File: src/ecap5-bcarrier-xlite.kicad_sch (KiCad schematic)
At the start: 41 parts, among them J3 Conn_01x04, J4 Conn_01x04, J5 USB_C_Receptacle_USB2.0_14P, J6 Conn_Coaxial, J7 Conn_Coaxial, J8 Conn_Coaxial, J9 1935161, Q1 BC846BR13, Q2 BC846BR13, SW1 RESET_SOM1, SW2 RESET_SOM2, SW3 USER1, SW4 USER1, U2 AP7375-33SA-7

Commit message: Route more
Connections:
- net GND: now also Q1.2 (E), Q2.2 (E); no longer Q1.E, Q2.E
- net at R11.1: now also Q2.1 (B); no longer Q2.B
- net at D8.1 (K): now also Q2.3 (C); no longer Q2.C
- net at D2.1 (K): now also Q1.3 (C); no longer Q1.C
- net at R9.1: now also Q1.1 (B); no longer Q1.B
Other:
- sheet SOM1 ports: added RTD0N, RTD0P, SE65; removed none
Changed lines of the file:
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@@
 	(wire
 		(pts
-			(xy 247.65 48.26) (xy 231.14 48.26)
+			(xy 241.3 48.26) (xy 224.79 48.26)
 		)
 		(stroke
@@
 	(wire
 		(pts
-			(xy 247.65 43.18) (xy 231.14 43.18)
+			(xy 241.3 43.18) (xy 224.79 43.18)
 		)
 		(stroke
@@
 	(wire
 		(pts
+			(xy 241.3 54.61) (xy 224.79 54.61)
+		)
+		(stroke
+			(width 0)
+			(type default)
+		)
+	)
+	(wire
+		(pts
 			(xy 52.07 74.93) (xy 57.15 74.93)
 		)
@@
 	(wire
 		(pts
-			(xy 247.65 45.72) (xy 231.14 45.72)
+			(xy 241.3 45.72) (xy 224.79 45.72)
 		)
 		(stroke
@@
 	(wire
 		(pts
+			(xy 241.3 58.42) (xy 224.79 58.42)
+		)
+		(stroke
+			(width 0)
+			(type default)
+		)
+	)
+	(wire
+		(pts
 			(xy 29.21 105.41) (xy 36.83 105.41)
 		)
@@
 	(wire
 		(pts
+			(xy 241.3 36.83) (xy 224.79 36.83)
+		)
+		(stroke
+			(width 0)
+			(type default)
+		)
+	)
+	(wire
+		(pts
 			(xy 158.75 153.67) (xy 154.94 153.67)
 		)
@@
 	(wire
 		(pts
+			(xy 241.3 52.07) (xy 224.79 52.07)
+		)
+		(stroke
+			(width 0)
+			(type default)
+		)
+	)
+	(wire
+		(pts
 			(xy 182.88 128.27) (xy 182.88 130.81)
 		)
@@
 	(wire
 		(pts
+			(xy 285.75 36.83) (xy 269.24 36.83)
+		)
+		(stroke
+			(width 0)
+			(type default)
+		)
+	)
+	(wire
+		(pts
 			(xy 250.19 149.86) (xy 254 149.86)
 		)
@@
 	(wire
 		(pts
-			(xy 247.65 40.64) (xy 231.14 40.64)
+			(xy 241.3 40.64) (xy 224.79 40.64)
 		)
 		(stroke
@@
 	)
 	(label "SOM1.JTAC_TDI"
-		(at 247.65 43.18 180)
+		(at 241.3 43.18 180)
 		(effects
 			(font
@@
 	)
 	(label "TP.SINGLEENDED"
-		(at 173.99 90.17 180)
+		(at 241.3 58.42 180)
 		(effects
 			(font
@@
 	)
 	(label "SOM1.JTAC_TCK"
-		(at 247.65 40.64 180)
+		(at 241.3 40.64 180)
 		(effects
 			(font
@@
 	)
 	(label "SOM1.JTAC_TMS"
-		(at 247.65 48.26 180)
+		(at 241.3 48.26 180)
 		(effects
 			(font
@@
 	)
 	(label "SOM1.JTAC_TDO"
-		(at 247.65 45.72 180)
+		(at 241.3 45.72 180)
 		(effects
 			(font
@@
 	)
 	(label "TP.DIFFN"
-		(at 173.99 95.25 180)
+		(at 241.3 54.61 180)
 		(effects
 			(font
@@
 	)
 	(label "TP.DIFFP"
-		(at 173.99 92.71 180)
+		(at 241.3 52.07 180)
 		(effects
 			(font
@@
 	)
 	(label "SOM2.RESET_IN"
-		(at 173.99 72.39 180)
+		(at 285.75 36.83 180)
 		(effects
 			(font
@@
 	)
 	(label "SOM1.RESET_IN"
-		(at 173.99 69.85 180)
+		(at 241.3 36.83 180)
 		(effects
 			(font
@@
 	)
 	(symbol
-		(lib_id "Device:Q_NPN")
-		(at 222.25 153.67 0)
-		(mirror y)
-		(unit 1)
-		(exclude_from_sim no)
-		(in_bom yes)
-		(on_board yes)
-		(dnp no)
-		(fields_autoplaced yes)
-		(property "Reference" "Q2"
-			(at 217.17 152.3999 0)
-			(effects
-				(font
-					(size 1.27 1.27)
-				)
-				(justify left)
-			)
-		)
-		(property "Value" "BC846BR13"
-			(at 217.17 154.9399 0)
-			(effects
-				(font
-					(size 1.27 1.27)
-				)
-				(justify left)
-			)
-		)
-		(property "Footprint" "Package_TO_SOT_SMD:SOT-23-3"
-			(at 217.17 151.13 0)
-			(effects
-				(font
-					(size 1.27 1.27)
-				)
-				(hide yes)
-			)
-		)
-		(property "Datasheet" "~"
-			(at 222.25 153.67 0)
-			(effects
-				(font
-					(size 1.27 1.27)
-				)
-				(hide yes)
-			)
-		)
-		(property "Description" "NPN bipolar junction transistor"
-			(at 222.25 153.67 0)
-			(effects
-				(font
-					(size 1.27 1.27)
-				)
-				(hide yes)
-			)
-		)
-		(pin "C"
-		)
-		(pin "B"
-		)
-		(pin "E"
-		)
-		(instances
-			(project "ecap5-bcarrier-xlite"
-				(path "/1031074d-9029-464c-8aee-89b18fdeb4ba"
-					(reference "Q2")
-					(unit 1)
-				)
-			)
-		)
-	)
-	(symbol
 		(lib_id "Switch:SW_Push")
 		(at 148.59 132.08 0)
@@
 	)
 	(symbol
+		(lib_name "Q_NPN_1")
 		(lib_id "Device:Q_NPN")
 		(at 185.42 153.67 0)
@@
 			)
 		)
-		(pin "C"
+		(pin "1"
 		)
-		(pin "B"
+		(pin "2"
 		)
-		(pin "E"
+		(pin "3"
 		)
 		(instances
@@
 	)
 	(symbol
+		(lib_name "Q_NPN_1")
+		(lib_id "Device:Q_NPN")
+		(at 222.25 153.67 0)
+		(mirror y)
+		(unit 1)
+		(exclude_from_sim no)
+		(in_bom yes)
+		(on_board yes)
+		(dnp no)
+		(fields_autoplaced yes)
+		(property "Reference" "Q2"
+			(at 217.17 152.3999 0)
+			(effects
+				(font
+					(size 1.27 1.27)
+				)
+				(justify left)
+			)
+		)
+		(property "Value" "BC846BR13"
+			(at 217.17 154.9399 0)
+			(effects
+				(font
+					(size 1.27 1.27)
+				)
+				(justify left)
+			)
+		)
+		(property "Footprint" "Package_TO_SOT_SMD:SOT-23-3"
+			(at 217.17 151.13 0)
+			(effects
+				(font
+					(size 1.27 1.27)
+				)
+				(hide yes)
+			)
+		)
+		(property "Datasheet" "~"
+			(at 222.25 153.67 0)
+			(effects
+				(font
+					(size 1.27 1.27)
+				)
+				(hide yes)
+			)
+		)
+		(property "Description" "NPN bipolar junction transistor"
+			(at 222.25 153.67 0)
+			(effects
+				(font
+					(size 1.27 1.27)
+				)
+				(hide yes)
+			)
+		)
+		(pin "1"
+		)
+		(pin "2"
+		)
+		(pin "3"
+		)
+		(instances
+			(project "ecap5-bcarrier-xlite"
+				(path "/1031074d-9029-464c-8aee-89b18fdeb4ba"
+					(reference "Q2")
+					(unit 1)
+				)
+			)
+		)
+	)
+	(symbol
 		(lib_id "Device:LED")
 		(at 219.71 142.24 90)
@@
 	)
 	(sheet
-		(at 210.82 34.29)
-		(size 20.32 20.32)
+		(at 204.47 34.29)
+		(size 20.32 31.75)
 		(exclude_from_sim no)
 		(in_bom yes)
@@
 		)
 		(property "Sheetname" "SOM1"
-			(at 210.82 33.5784 0)
+			(at 204.47 33.5784 0)
 			(effects
 				(font
@@
 		)
 		(property "Sheetfile" "schematics/som1.kicad_sch"
-			(at 210.82 55.1946 0)
+			(at 204.47 66.6246 0)
 			(effects
 				(font
@@
 		)
 		(pin "JTAG_TCK" input
-			(at 231.14 40.64 0)
+			(at 224.79 40.64 0)
 			(effects
 				(font
@@
 		)
 		(pin "JTAG_TDI" input
-			(at 231.14 43.18 0)
+			(at 224.79 43.18 0)
 			(effects
 				(font
@@
 		)
 		(pin "JTAG_TDO" input
-			(at 231.14 45.72 0)
+			(at 224.79 45.72 0)
 			(effects
 				(font
@@
 		)
 		(pin "JTAG_TMS" input
-			(at 231.14 48.26 0)
+			(at 224.79 48.26 0)
 			(effects
 				(font
@@
 		)
 		(pin "RESET_IN" input
-			(at 231.14 36.83 0)
+			(at 224.79 36.83 0)
+			(effects
+				(font
+					(size 1.27 1.27)
+				)
+				(justify right)
+			)
+		)
+		(pin "RTD0N" input
+			(at 224.79 54.61 0)
+			(effects
+				(font
+					(size 1.27 1.27)
+				)
+				(justify right)
+			)
+		)
+		(pin "RTD0P" input
+			(at 224.79 52.07 0)
+			(effects
+				(font
+					(size 1.27 1.27)
+				)
+				(justify right)
+			)
+		)
+		(pin "SE65" input
+			(at 224.79 58.42 0)
 			(effects
 				(font

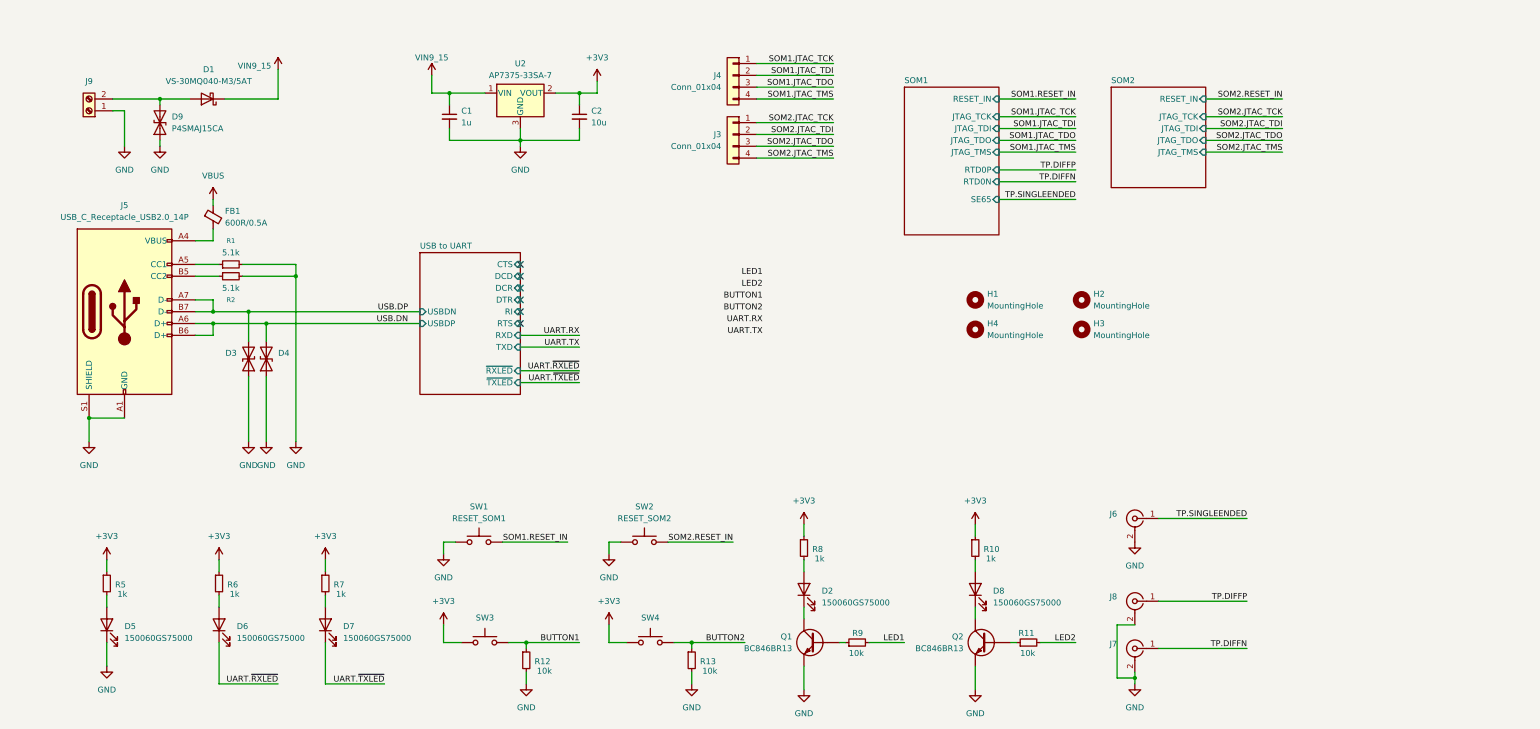
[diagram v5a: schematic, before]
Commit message: Route the LVDS pairs
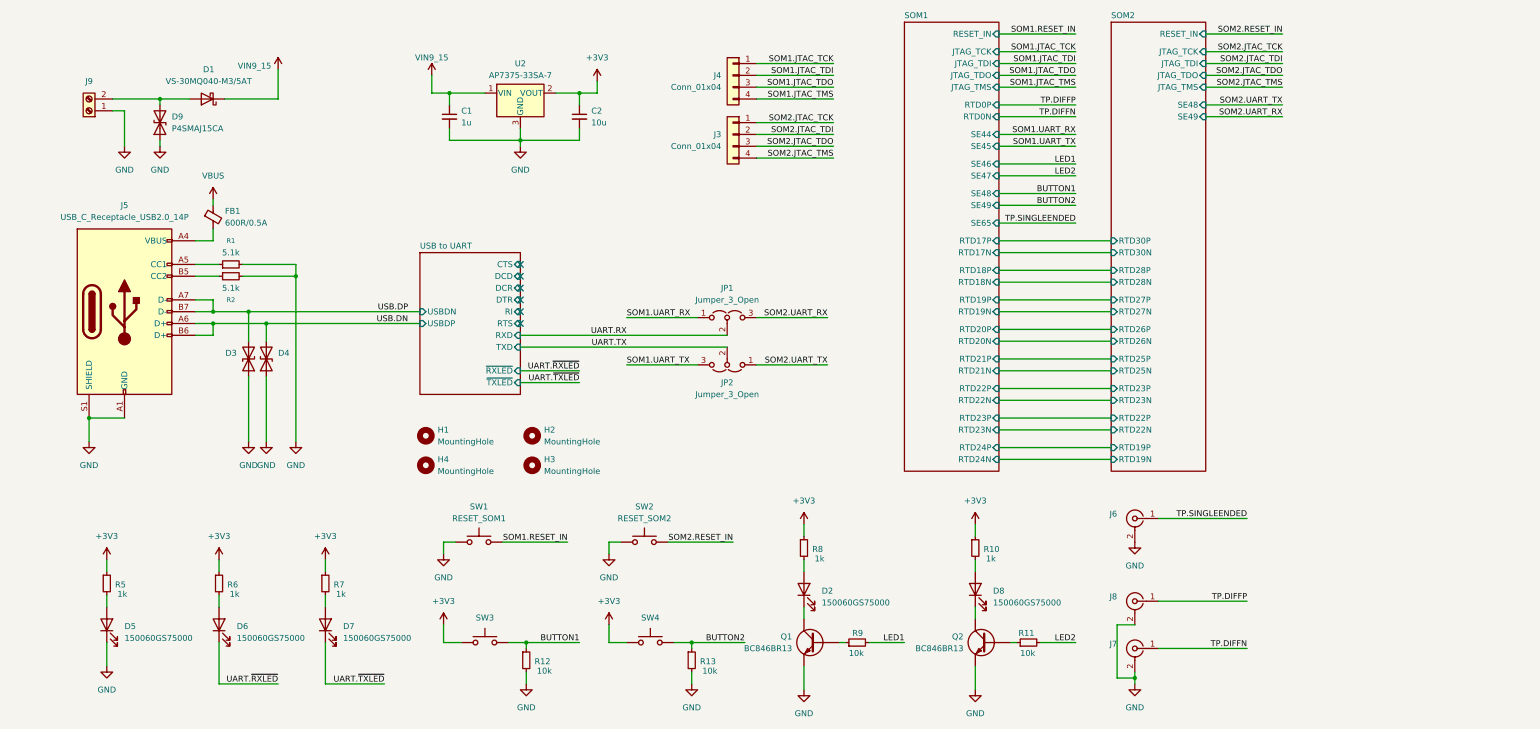
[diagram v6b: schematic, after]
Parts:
- added JP1, JP2: Jumper_3_Open, Connector_PinHeader_2.54mm:PinHeader_1x03_P2.54mm_Vertical, symbol Jumper:Jumper_3_Open
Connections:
- net UART.RX: now also JP1.2 (C)
- net UART.TX: now also JP2.2 (C)
- new net SOM1.UART_RX: JP1.1 (A)
- new net SOM1.UART_TX: JP2.3 (B)
- new net SOM2.UART_RX: JP1.3 (B)
- new net SOM2.UART_TX: JP2.1 (A)
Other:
- sheet SOM1 ports: added RTD17N, RTD17P, RTD18N, RTD18P, RTD19N, RTD19P, RTD20N, RTD20P, RTD21N, RTD21P, RTD22N, RTD22P, RTD23N, RTD23P, RTD24N, RTD24P, SE44, SE45, SE46, SE47, SE48, SE49; removed none
- sheet SOM2 ports: added RTD19N, RTD19P, RTD22N, RTD22P, RTD23N, RTD23P, RTD25N, RTD25P, RTD26N, RTD26P, RTD27N, RTD27P, RTD28N, RTD28P, RTD30N, RTD30P, SE48, SE49; removed none
- moved on the sheet: H1, H2, H3, H4

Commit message: Finish routing the single-ended signals
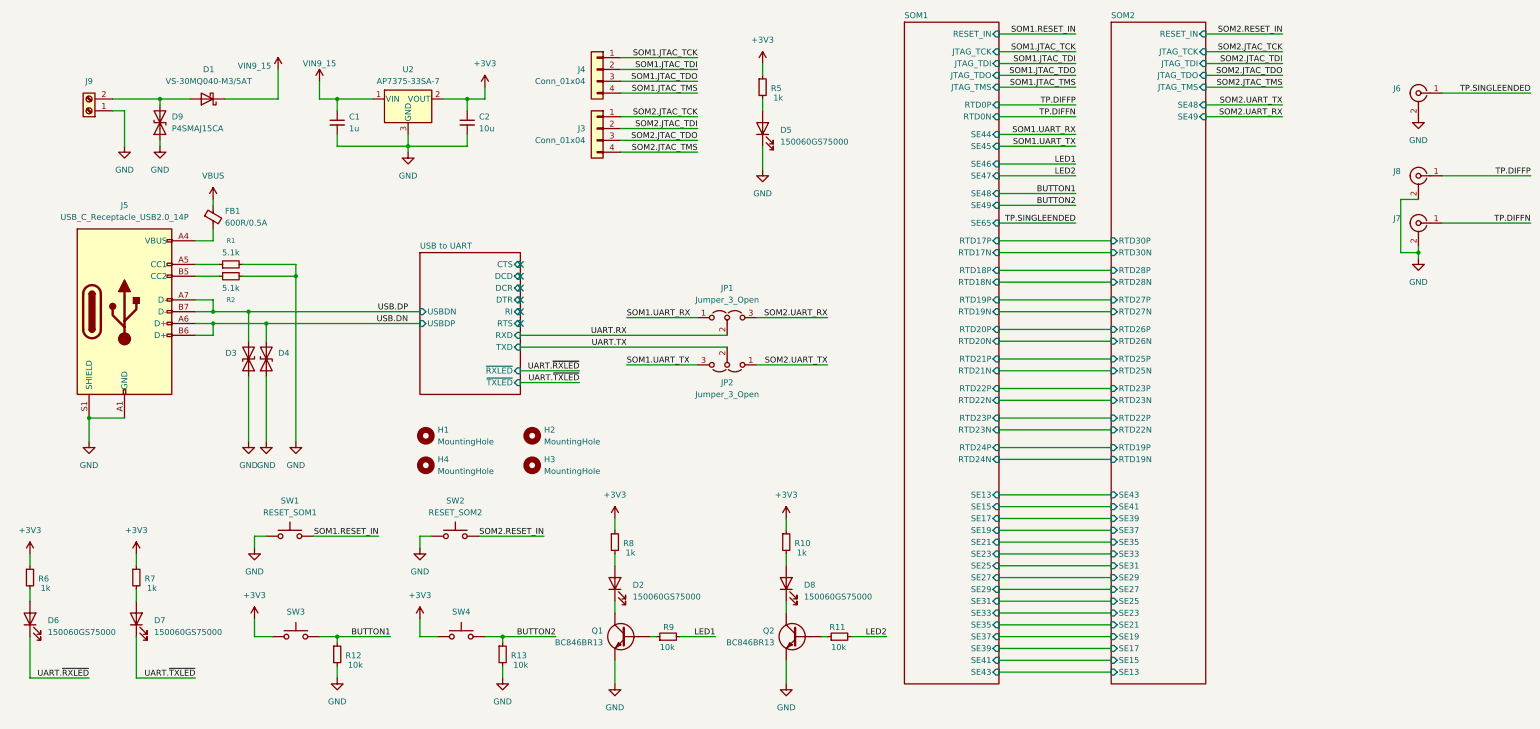
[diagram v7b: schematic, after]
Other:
- sheet SOM1 ports: added SE13, SE15, SE17, SE19, SE21, SE23, SE25, SE27, SE29, SE31, SE33, SE35, SE37, SE39, SE41, SE43; removed none
- sheet SOM2 ports: added SE13, SE15, SE17, SE19, SE21, SE23, SE25, SE27, SE29, SE31, SE33, SE35, SE37, SE39, SE41, SE43; removed none
- moved on the sheet: C1, C2, D2, D5, D6, D7, D8, J3, J4, J6, J7, J8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

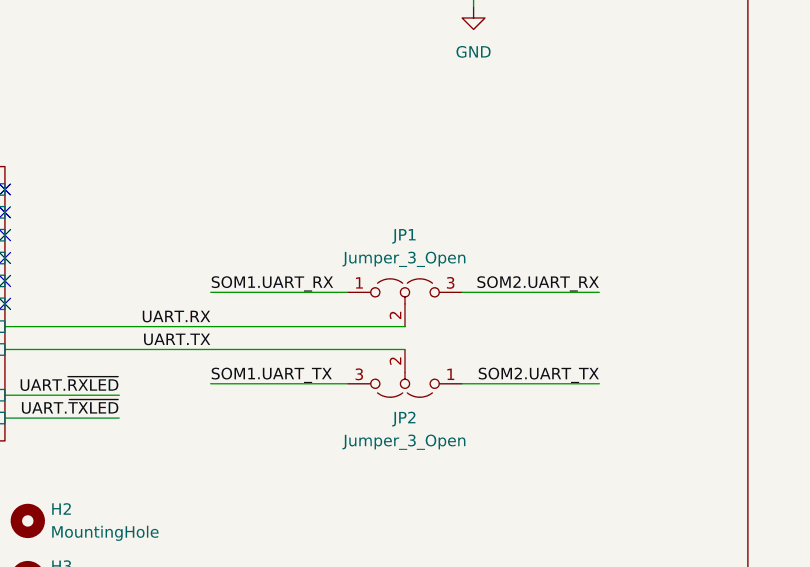
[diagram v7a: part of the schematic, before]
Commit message: Start adding silkscreen
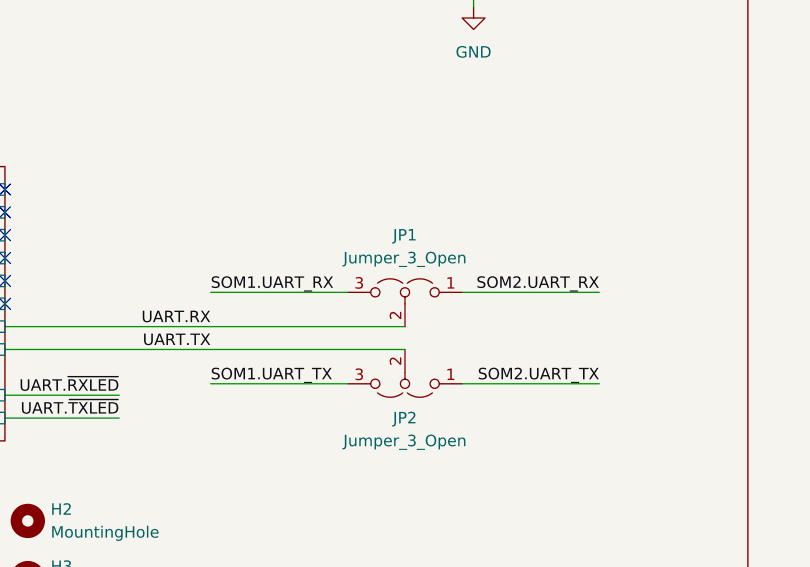
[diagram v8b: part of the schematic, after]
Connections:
- net SOM1.UART_RX: now also JP1.3 (B); no longer JP1.1 (A)
- net SOM2.UART_RX: now also JP1.1 (A); no longer JP1.3 (B)
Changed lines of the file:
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@@
 		(lib_id "Jumper:Jumper_3_Open")
 		(at 166.37 83.82 0)
+		(mirror y)
 		(unit 1)
 		(exclude_from_sim no)
@@
 		(on_board yes)
 		(dnp no)
-		(fields_autoplaced yes)
 		(property "Reference" "JP1"
 			(at 166.37 77.47 0)
@@
 		(on_board yes)
 		(dnp no)
-		(fields_autoplaced yes)
 		(property "Reference" "JP2"
 			(at 166.37 97.79 0)
